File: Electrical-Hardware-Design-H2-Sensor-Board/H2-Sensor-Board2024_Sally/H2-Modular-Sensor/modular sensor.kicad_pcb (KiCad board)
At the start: 2 copper layers, 31.8 x 20.3 mm, 11 parts, among them J1 Conn_01x03, U1 LM317_HORIZONTAL, U2 MCP6007

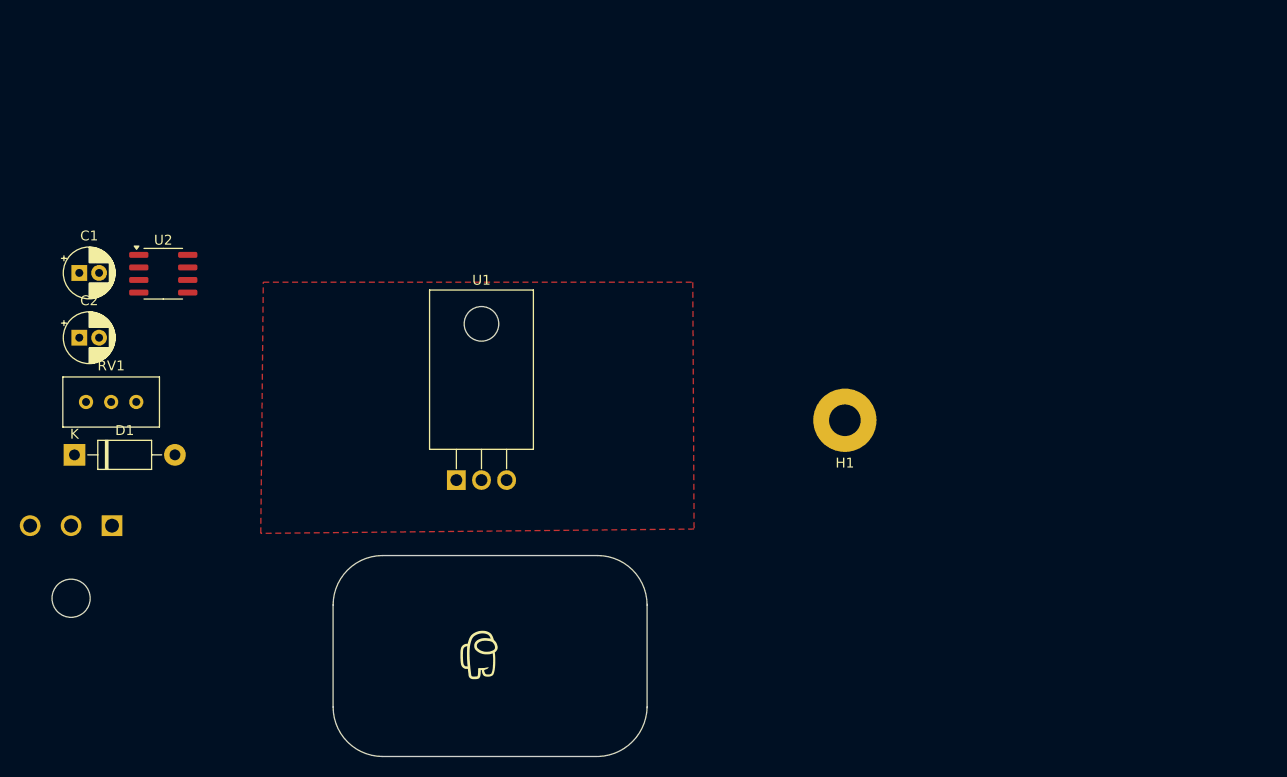
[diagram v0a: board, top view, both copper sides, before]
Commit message: MoSen layout - finish floorplan
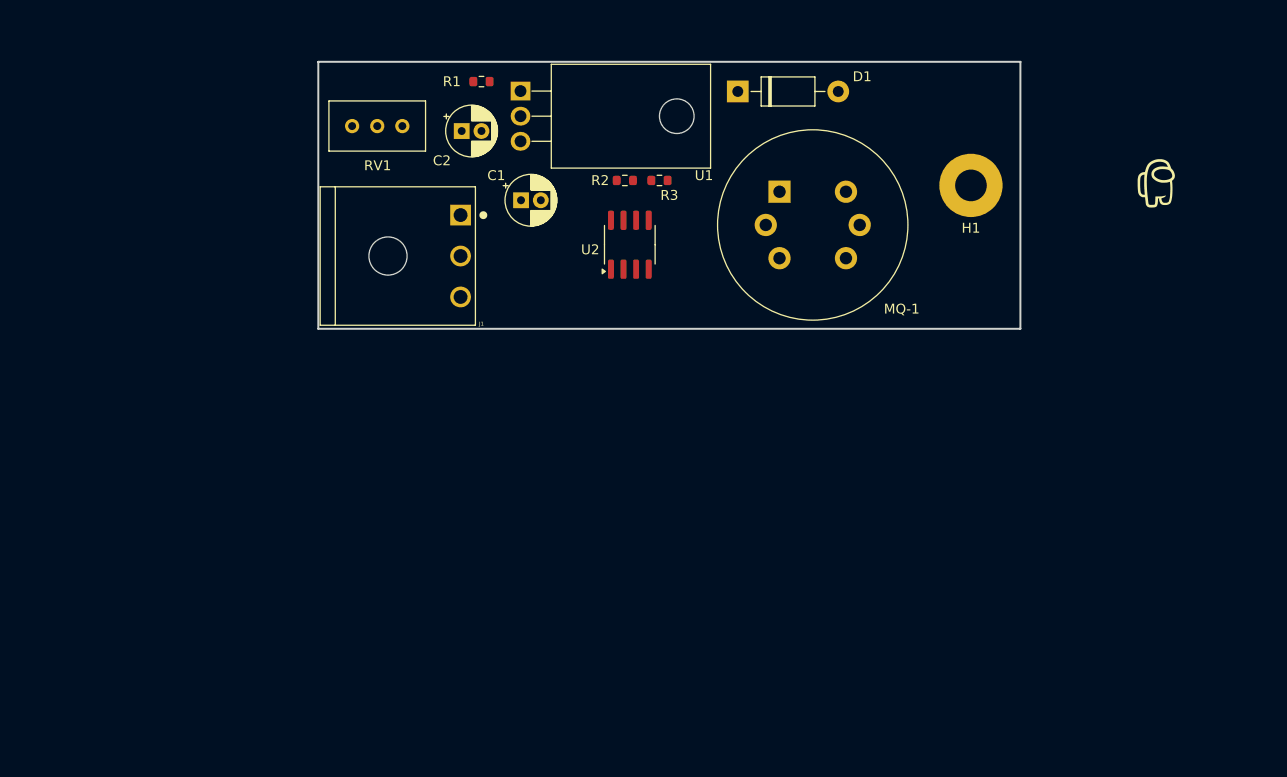
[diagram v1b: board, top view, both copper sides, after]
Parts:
- added MQ-1: MQ-8, Modular sensor footprints:MQ-8, F.Cu at (175.1, 72.6)
- added R1: 330, Resistor_SMD:R_0603_1608Metric, F.Cu at (145.0, 61.5)
- added R2: 100, Resistor_SMD:R_0603_1608Metric, F.Cu at (159.5, 71.5)
- added R3: 100, Resistor_SMD:R_0603_1608Metric, F.Cu at (163.0, 71.5)
- J1: moved to F.Cu
- moved G*** 83.5 mm to (213.2, 71.8)
- moved G*** 83.5 mm to (217.6, 64.1)
- moved G*** 83.5 mm to (220.1, 64.1)
- moved D1 76.5 mm to (170.9, 62.5)
- moved J1 47.9 mm to (142.9, 79.1), turned to -90 degrees
- moved U2 47.3 mm to (160.0, 78.0), turned to 90 degrees
- moved C1 45.3 mm to (149.0, 73.5)
- moved C2 44.0 mm to (143.0, 66.5)
- moved U1 39.9 mm to (148.9, 62.5), turned to -90 degrees
- moved RV1 35.4 mm to (131.9, 66.0), turned to 180 degrees
- moved H1 27.0 mm to (194.5, 72.0)
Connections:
- net Net-(U2B--) renamed /MCP6007B-
- J1 pad 2: /V_RL -> /V_Sensed
- U2 pad 5: Net-(U2B-+) -> /MCP6007B+
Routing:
- removed copper zone on F.Cu, net GND
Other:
- board size 31.8 x 20.3 mm -> 71 x 27 mm
- rule pad_to_mask_clearance: 0 -> 0.038
- board text added: "GND"
- board text added: "H2 MoSen ${REVISION}"
- board text added: "Owen W. || 01/25"
- board text removed: "H2 Sensor Daughter Board ${REVISION}"
- board text removed: "Simon W."

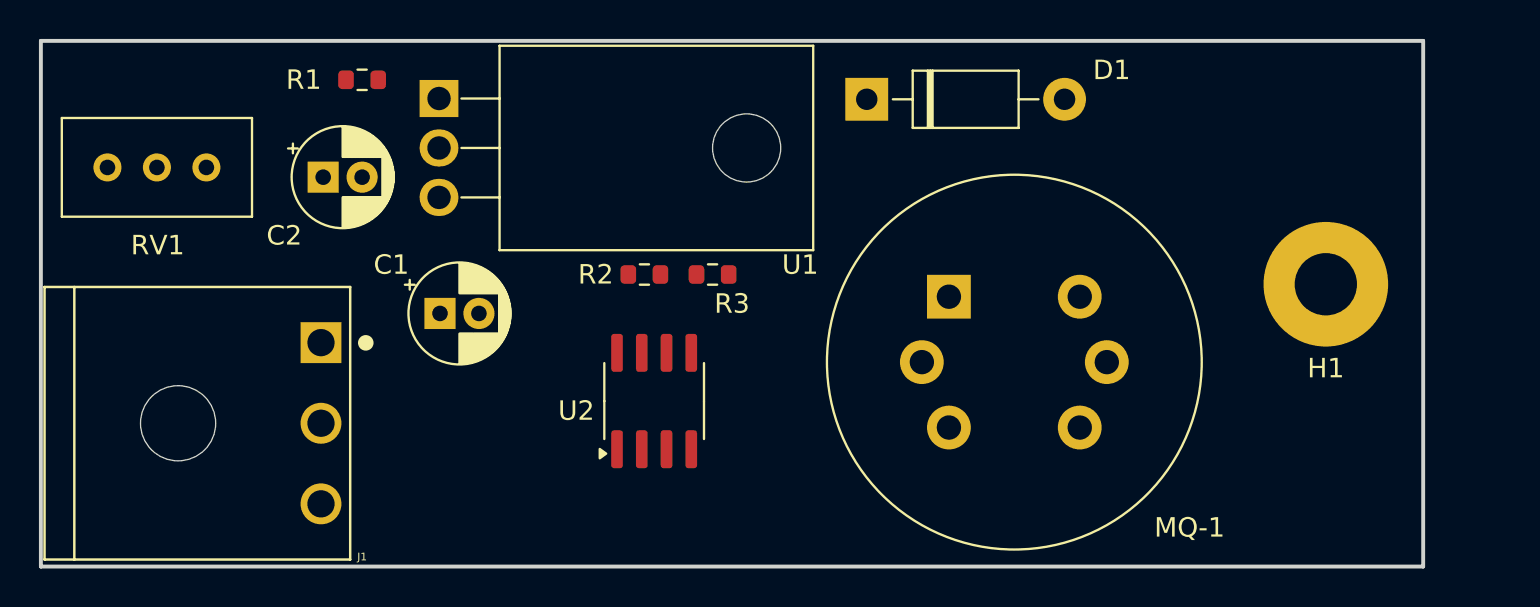
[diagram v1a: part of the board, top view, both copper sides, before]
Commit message: change MoSen voltage reg ckt
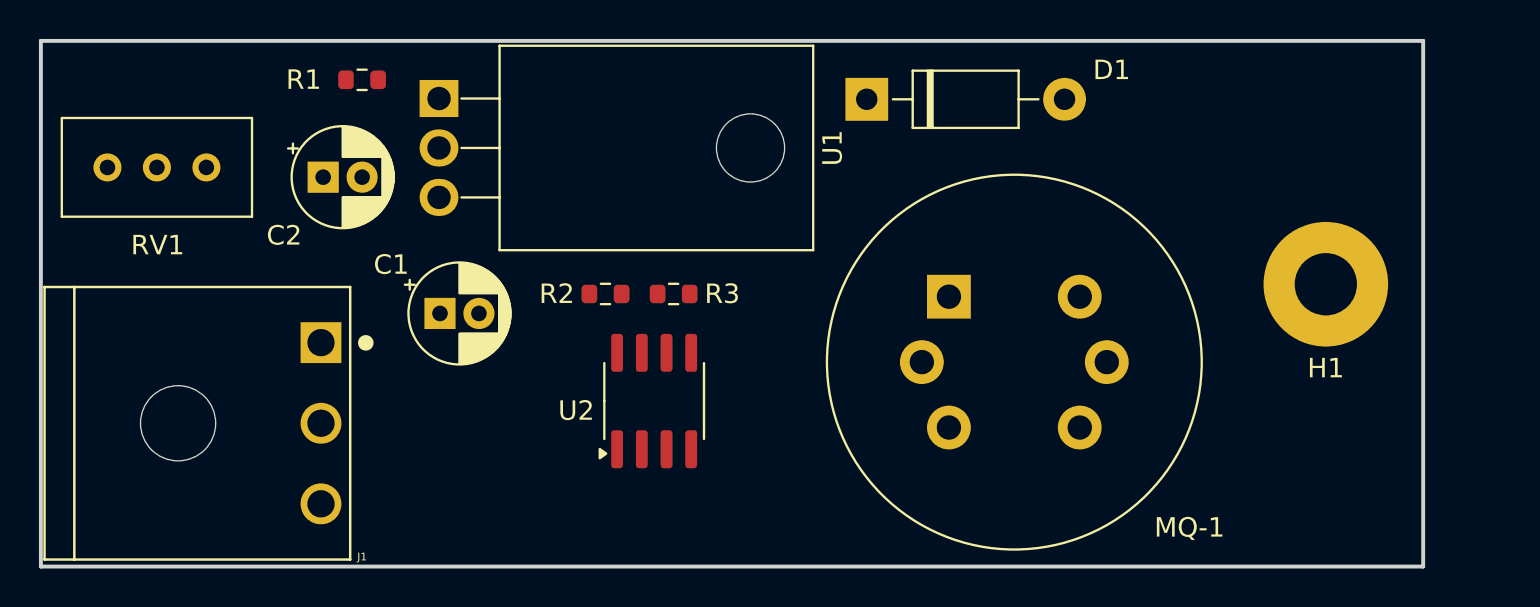
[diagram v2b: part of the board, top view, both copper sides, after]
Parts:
- U1: footprint Package_TO_SOT_THT:TO-220F-3_Horizontal_TabDown -> ecocad_lib_footprints:LM317FP_tabdown
- moved R2 2.24 mm to (157.5, 72.5)
- moved R3 2.24 mm to (161.0, 72.5)
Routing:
- added copper zone on B.Cu, net GND
- added copper zone on F.Cu, net GND
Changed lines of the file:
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@@
 		(tags "CP Radial series Radial pin pitch 2.00mm  diameter 5mm Electrolytic Capacitor")
 		(property "Reference" "C1"
-			(at -2.5 -2.5 360)
+			(at -2.5 -2.5 0)
 			(layer "F.SilkS")
 			(effects
@@
 		)
 		(property "Value" "0u1"
-			(at 1 3.75 360)
+			(at 1 3.75 0)
 			(layer "F.Fab")
 			(effects
@@
 		)
 		(fp_text user "${REFERENCE}"
-			(at 1 0 360)
+			(at 1 0 0)
 			(layer "F.Fab")
 			(effects
@@
 	(footprint "Resistor_SMD:R_0603_1608Metric"
 		(layer "F.Cu")
-		(at 159.5 71.5 180)
+		(at 157.5 72.5 180)
 		(descr "Resistor SMD 0603 (1608 Metric), square (rectangular) end terminal, IPC_7351 nominal, (Body size source: IPC-SM-782 page 72, https://www.pcb-3d.com/wordpress/wp-content/uploads/ipc-sm-782a_amendment_1_and_2.pdf), generated with kicad-footprint-generator")
 		(tags "resistor")
 		(property "Reference" "R2"
-			(at 2.5 0 360)
+			(at 2.5 0 0)
 			(layer "F.SilkS")
 			(effects
@@
 		)
 		(property "Value" "100"
-			(at 0 1.43 360)
+			(at 0 1.43 0)
 			(layer "F.Fab")
 			(effects
@@
 		)
 		(fp_text user "${REFERENCE}"
-			(at 0 0 360)
+			(at 0 0 0)
 			(layer "F.Fab")
 			(effects
@@
 	(footprint "Resistor_SMD:R_0603_1608Metric"
 		(layer "F.Cu")
-		(at 163 71.5 180)
+		(at 161 72.5 180)
 		(descr "Resistor SMD 0603 (1608 Metric), square (rectangular) end terminal, IPC_7351 nominal, (Body size source: IPC-SM-782 page 72, https://www.pcb-3d.com/wordpress/wp-content/uploads/ipc-sm-782a_amendment_1_and_2.pdf), generated with kicad-footprint-generator")
 		(tags "resistor")
 		(property "Reference" "R3"
-			(at -1 -1.5 180)
+			(at -2.5 0 180)
 			(layer "F.SilkS")
 			(effects
@@
 		)
 		(property "Value" "100"
-			(at 0 1.43 360)
+			(at 0 1.43 0)
 			(layer "F.Fab")
 			(effects
@@
 		)
 		(fp_text user "${REFERENCE}"
-			(at 0 0 360)
+			(at 0 0 0)
 			(layer "F.Fab")
 			(effects
@@
 		)
 	)
-	(footprint "Package_TO_SOT_THT:TO-220F-3_Horizontal_TabDown"
+	(footprint "ecocad_lib_footprints:LM317FP_tabdown"
 		(layer "F.Cu")
 		(at 148.95 62.46 -90)
@@
 		(tags "TO-220F-3 Horizontal RM 2.54mm")
 		(property "Reference" "U1"
-			(at 8.54 -18.55 180)
+			(at 2.54 -20.22 90)
 			(layer "F.SilkS")
 			(effects
@@
 			)
 		)
-		(property "Footprint" "Package_TO_SOT_THT:TO-220F-3_Horizontal_TabDown"
+		(property "Footprint" "ecocad_lib_footprints:LM317FP_tabdown"
 			(at 0 0 -90)
 			(unlocked yes)
@@
 		)
 		(fp_circle
-			(center 2.54 -15.8)
-			(end 4.39 -15.8)
+			(center 2.54 -16)
+			(end 4.39 -16)
 			(stroke
 				(width 0.1)
@@
 		)
 		(pad "" np_thru_hole oval
-			(at 2.54 -15.8 270)
+			(at 2.54 -16 270)
 			(size 3.5 3.5)
 			(drill 3.5)
@@
 		(tags "CP Radial series Radial pin pitch 2.00mm  diameter 5mm Electrolytic Capacitor")
 		(property "Reference" "C2"
-			(at -2 3 360)
+			(at -2 3 0)
 			(layer "F.SilkS")
 			(effects
@@
 		)
 		(property "Value" "10u"
-			(at 1 3.75 360)
+			(at 1 3.75 0)
 			(layer "F.Fab")
 			(effects
@@
 		)
 		(fp_text user "${REFERENCE}"
-			(at 1 0 360)
+			(at 1 0 0)
 			(layer "F.Fab")
 			(effects
@@
 		(tags "Diode DO-41_SOD81 series Axial Horizontal pin pitch 10.16mm  length 5.2mm diameter 2.7mm")
 		(property "Reference" "D1"
-			(at 12.58 -1.5 360)
+			(at 12.58 -1.5 0)
 			(layer "F.SilkS")
 			(effects
@@
 		)
 		(property "Value" "1N4733"
-			(at 5.08 2.47 360)
+			(at 5.08 2.47 0)
 			(layer "F.Fab")
 			(effects
@@
 		)
 		(fp_text user "${REFERENCE}"
-			(at 5.47 0 360)
+			(at 5.47 0 0)
 			(layer "F.Fab")
 			(effects
@@
 		)
 		(fp_text user "K"
-			(at 0 -2.1 360)
+			(at 0 -2.1 0)
 			(layer "F.Fab")
 			(effects
@@
 		(tags "gas sensor")
 		(property "Reference" "MQ-1"
-			(at 12.36 11.86 360)
+			(at 12.36 11.86 0)
 			(layer "F.SilkS")
 			(effects
@@
 		)
 		(property "Value" "MQ-8"
-			(at 3.36 14.36 360)
+			(at 3.36 14.36 0)
 			(layer "F.Fab")
 			(effects
@@
 		)
 		(property "Footprint" "Modular sensor footprints:MQ-8"
-			(at 0 0 360)
+			(at 0 0 0)
 			(layer "F.Fab")
 			(hide yes)
@@
 		)
 		(property "Datasheet" "https://www.winsen-sensor.com/d/files/mq-8-(ver1_6)---manual.pdf"
-			(at 0 0 360)
+			(at 0 0 0)
 			(layer "F.Fab")
 			(hide yes)
@@
 		)
 		(property "Description" "Semiconductor Sensor for Flammable Gas"
-			(at 0 0 360)
+			(at 0 0 0)
 			(layer "F.Fab")
 			(hide yes)
@@
 		)
 		(fp_text user "${REFERENCE}"
-			(at 3.65 10.16 360)
+			(at 3.65 10.16 0)
 			(layer "F.Fab")
 			(effects
@@
 		(tags "SOIC SO")
 		(property "Reference" "U2"
-			(at -0.5 -4 360)
+			(at -0.5 -4 0)
 			(layer "F.SilkS")
 			(effects
@@
 		(tags "resistor")
 		(property "Reference" "R1"
-			(at -3 0 360)
+			(at -3 0 0)
 			(layer "F.SilkS")
 			(effects
@@
 		)
 		(property "Value" "330"
-			(at 0 1.43 360)
+			(at 0 1.43 0)
 			(layer "F.Fab")
 			(effects
@@
 		)
 		(fp_text user "${REFERENCE}"
-			(at 0.075 0.02 360)
+			(at 0.075 0.02 0)
 			(layer "F.Fab")
 			(effects
@@
 		)
 	)
+	(zone
+		(net 2)
+		(net_name "GND")
+		(layer "F.Cu")
+		(hatch edge 0.5)
+		(connect_pads
+			(clearance 0.3)
+		)
+		(min_thickness 0.25)
+		(filled_areas_thickness no)
+		(fill yes
+			(thermal_gap 0.5)
+			(thermal_bridge_width 0.5)
+		)
+		(polygon
+			(pts
+				(xy 128.5 59.5) (xy 199.5 59.5) (xy 199.5 86.5) (xy 128.5 86.5) (xy 128.5 70)
+			)
+		)
+	)
+	(zone
+		(net 2)
+		(net_name "GND")
+		(layer "B.Cu")
+		(hatch edge 0.5)
+		(priority 1)
+		(connect_pads
+			(clearance 0.3)
+		)
+		(min_thickness 0.25)
+		(filled_areas_thickness no)
+		(fill yes
+			(thermal_gap 0.5)
+			(thermal_bridge_width 0.5)
+		)
+		(polygon
+			(pts
+				(xy 199.5 59.5) (xy 128.5 59.5) (xy 128.5 86.5) (xy 199.5 86.5)
+			)
+		)
+	)

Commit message: update to layout
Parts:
- removed R3: 100, Resistor_SMD:R_0603_1608Metric
- removed RV1: 2k, Potentiometer_THT:Potentiometer_Bourns_3296W_Vertical
- C1: value 0u1 -> 10u; footprint Capacitor_THT:CP_Radial_D5.0mm_P2.00mm -> Capacitor_SMD:C_0603_1608Metric
- C2: value 10u -> 22u; footprint Capacitor_THT:CP_Radial_D5.0mm_P2.00mm -> Capacitor_SMD:C_0603_1608Metric
- R1: value 330 -> 100
- U1: value LM317_HORIZONTAL -> AZ1117IH-5.0; footprint ecocad_lib_footprints:LM317FP_tabdown -> Package_TO_SOT_SMD:SOT-223-3_TabPin2
- moved C1 19.6 mm to (132.5, 63.0), turned to 90 degrees
- moved C2 16.0 mm to (129.5, 58.0)
- moved J1 15.6 mm to (129.0, 72.0)
- moved H1 13.9 mm to (180.6, 71.6)
- moved R2 13.9 mm to (143.6, 72.1)
- moved U2 13.9 mm to (146.1, 77.6)
- moved D1 13.9 mm to (157.1, 62.1)
- moved MQ-1 13.9 mm to (161.3, 72.3)
- moved R1 10.3 mm to (154.7, 58.0)
- moved U1 7.89 mm to (142.5, 67.0), turned to 0 degrees
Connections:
- R1 pad 1: /V_Heater -> /MCP6007B+
- R1 pad 2: Net-(U1-ADJ) -> /V_Heater
- R2 pad 1: /MCP6007B+ -> GND
- R2 pad 2: /V_Heater -> /MCP6007B+
- U1 pad 1: Net-(U1-ADJ) -> GND

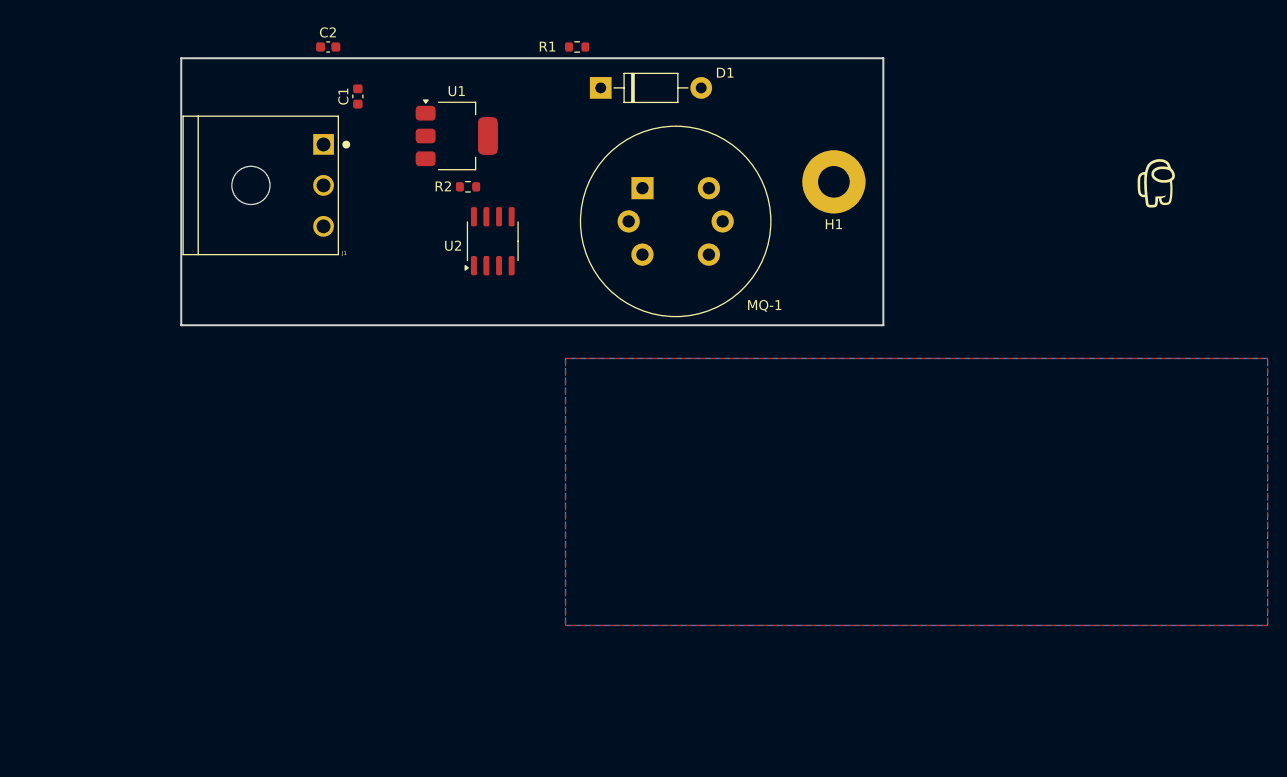
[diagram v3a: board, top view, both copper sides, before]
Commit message: finish H2 MoSen layout
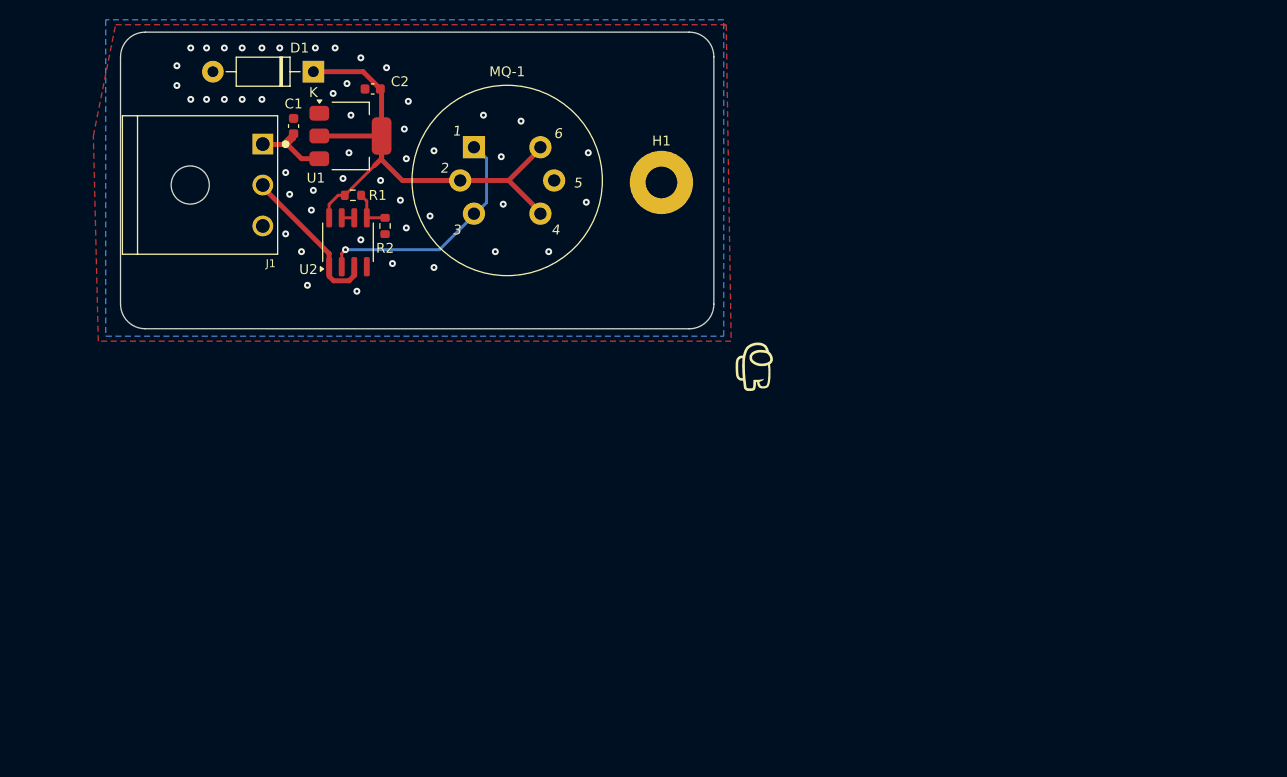
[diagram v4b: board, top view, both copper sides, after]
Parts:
- moved G*** 61.9 mm to (158.4, 59.3)
- moved G*** 61.8 mm to (156.0, 59.3)
- moved G*** 44.7 mm to (172.6, 90.3)
- moved D1 29.1 mm to (128.0, 60.5), turned to 180 degrees
- moved R1 27.2 mm to (132.0, 73.0), turned to 180 degrees
- moved MQ-1 17.5 mm to (144.2, 68.1)
- moved H1 17.4 mm to (163.2, 71.7)
- moved U2 14.6 mm to (131.5, 77.8)
- moved U1 10.8 mm to (131.8, 67.0)
- moved R2 9.28 mm to (135.2, 76.1), turned to 90 degrees
- moved C1 7.16 mm to (126.0, 66.0)
- moved C2 6.19 mm to (134.0, 62.2), turned to 180 degrees
- moved J1 6.14 mm to (122.9, 72.0)
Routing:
- net /V_Heater: track 0.00 -> 55.0 mm
- net /V_RL: track 0.00 -> 24.2 mm, vias 0 -> 1
- net /V_Sensed: track 0.00 -> 16.4 mm
- net /H2_PWR_unfilter: track 0.00 -> 9.21 mm
- net /MCP6007B+: track 0.00 -> 4.36 mm
- net /MCP6007B-: track 0.00 -> 1.27 mm
- net GND: vias 0 -> 49
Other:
- board size 71 x 27 mm -> 60 x 30 mm
- board text added: "1"
- board text added: "2"
- board text added: "3"
- board text added: "4"
- board text added: "5"
- board text added: "6"
- board text added: "H2 MoSen R${REVISION}"
- board text added: "Owen W. || 01.25 || Sally"
- board text removed: "H2 MoSen ${REVISION}"
- board text removed: "Owen W. || 01/25"

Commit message: layout update
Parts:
- added H2: MountingHole_Pad, MountingHole:MountingHole_3.2mm_M3_Pad, F.Cu at (139.2, 82.8)
- added H3: MountingHole_Pad, MountingHole:MountingHole_3.2mm_M3_Pad, F.Cu at (139.2, 60.5)
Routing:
- net GND: vias 49 -> 51

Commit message: end-of-day update
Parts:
- J1: value Conn_01x03 -> Molex_6_Pin; footprint ecocad_lib_footprints:TE_1-770967-0 -> ecocad_lib_footprints:Molex_6_pin_RightAngle
- moved J1 4.84 mm to (119.2, 75.1)
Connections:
- J1 pad 1: /H2_PWR_unfilter -> GND
- J1 pad 2: /V_Sensed -> /H2_PWR_unfilter
- J1 pad 3: GND -> /V_Sensed
